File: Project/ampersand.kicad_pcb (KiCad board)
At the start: 2 copper layers, 257.2 x 76.2 mm, 121 parts, among them J1 JST SH, SW1 DFU, U1 STM32F072CBT6, U2 XC6206PxxxMR-Regulator_Linear, U3 74HC4051, U4 OPA354, U5 74HC4051

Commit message: initialise
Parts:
- C11, C12, C14, C6: value 100n -> 100nF
- C7: value 1u -> 1uF
- moved C8 3.97 mm to (92.8, 96.5)
- moved R19 2.72 mm to (199.8, 85.5)
- moved C1 2.58 mm to (91.3, 87.4)
- moved C7 2.58 mm to (91.3, 86.4)
- moved R15 2.45 mm to (198.4, 85.4), turned to 90 degrees
- moved R20 1.71 mm to (197.7, 93.4), turned to -90 degrees
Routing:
- net NRST: track 1.73 -> 5.34 mm
- net +3V3: track 275.4 -> 278.2 mm
- net GND: track 77.1 -> 75.3 mm, vias 418 -> 412
- net COL11: track 161.8 -> 163.3 mm
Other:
- board text added: "6 7 10"
- board text removed: "6 7 8 10"

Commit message: pcb & plate revisions & firmware
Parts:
- added H19: MountingHole, cipulot_parts:HOLE_M2, F.Cu at (69.8, 91.3)
- added H20: MountingHole, cipulot_parts:HOLE_M2, F.Cu at (222.2, 91.3)
- SW_EC40, SW_EC49: footprint cipulot_parts:ecs_pad_no_ring_stepped&normal_cut -> cipulot_parts:ecs_pad_1U_no_ring
- moved SW_EC40 4.76 mm to (60.3, 91.3), turned to -90 degrees
- moved H14 1.59 mm to (88.9, 91.3)
- moved H15 1.59 mm to (203.2, 91.3)
- turned SW_EC49 to -90 degrees
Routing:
- net ROW3: track 397.8 -> 388.7 mm, vias 12 -> 10
- net Net-(U1-PB4): track 46.1 -> 47.4 mm
- net COL10: track 102.7 -> 101.6 mm, vias 5 -> 4
- net COL1: track 72.0 -> 71.6 mm, vias 5 -> 4
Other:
- board text added: "6"
- board text removed: "6 7 10"

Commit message: bottom row change, plate update, firmware update
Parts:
- added H26: MountingHole, cipulot_parts:HOLE_M2, F.Cu at (212.7, 91.3)
- added H27: MountingHole, cipulot_parts:HOLE_M2, F.Cu at (79.4, 91.3)
- moved G*** 75.2 mm to (141.3, 42.9)
- moved H14 33.3 mm to (55.6, 91.3)
- moved SW1 29.0 mm to (186.2, 96.8), turned to 90 degrees
- moved H19 28.6 mm to (98.4, 91.3)
- moved C7 19.6 mm to (109.2, 94.2), turned to 0 degrees
- moved C1 18.8 mm to (109.2, 93.2), turned to 0 degrees
- moved C3 17.9 mm to (111.3, 89.6), turned to 90 degrees
- moved C8 17.6 mm to (109.9, 92.1), turned to 0 degrees
- moved R5 17.3 mm to (111.3, 87.7), turned to -90 degrees
- moved C4 16.8 mm to (109.9, 91.0), turned to 0 degrees
- moved C13 16.3 mm to (101.6, 96.5), turned to 90 degrees
- moved C2 16.0 mm to (110.0, 82.2), turned to -90 degrees
- moved R11 16.0 mm to (107.3, 94.2), turned to 180 degrees
- moved U4 15.3 mm to (104.0, 95.8), turned to 90 degrees
- moved R13 15.1 mm to (107.3, 93.1), turned to 180 degrees
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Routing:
- net Net-(U1-PB6): track 48.2 -> 22.7 mm
- net Net-(U1-PB4): track 47.4 -> 22.1 mm
- net Net-(U1-PB5): track 47.1 -> 22.4 mm
- net Net-(U1-PB3): track 44.9 -> 21.8 mm
- net D_P: track 121.3 -> 105.8 mm
- net D_N: track 117.6 -> 102.8 mm
- net +3V3: track 278.2 -> 264.7 mm, vias 9 -> 8
- net ADC: track 5.95 -> 15.9 mm
- net COL6: track 110.6 -> 101.1 mm
- net COL11: track 163.3 -> 172.5 mm
- net GND: track 75.3 -> 84.0 mm, vias 412 -> 411
- net COL2: track 92.7 -> 101.1 mm
- net BOOT0: track 81.8 -> 89.6 mm
- net AMUX_SEL_0: track 172.7 -> 165.5 mm
- net AMUX_SEL_1: track 171.9 -> 165.0 mm
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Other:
- board text added: "7 10"
- board text removed: "3"
- board text removed: "6"

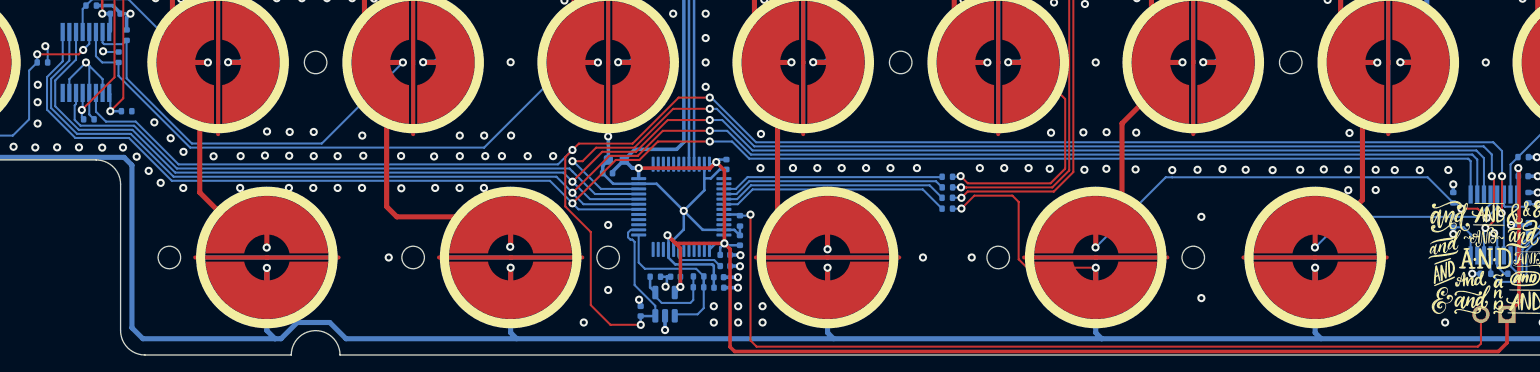
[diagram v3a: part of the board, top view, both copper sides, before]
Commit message: updated production files
naevies plate added
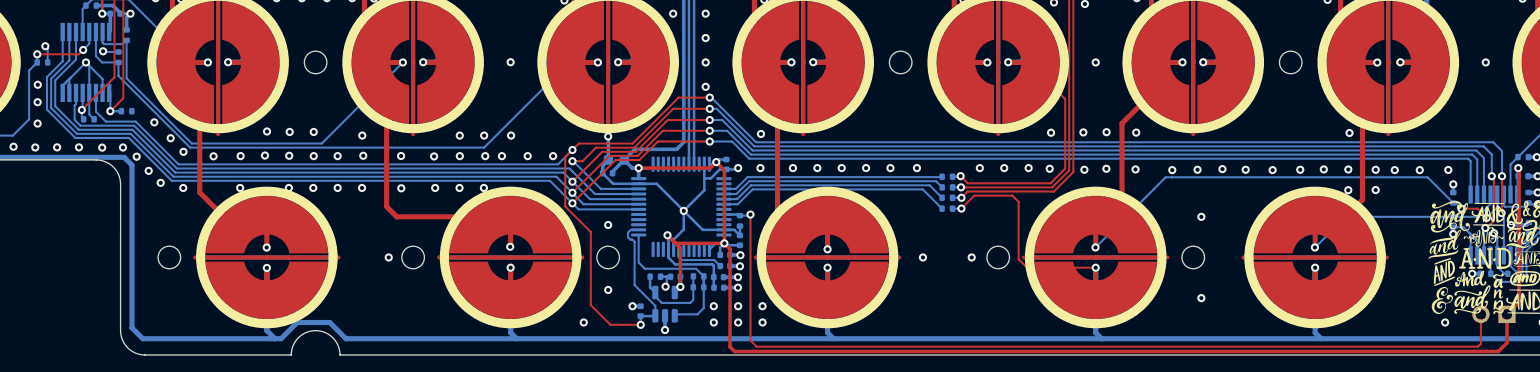
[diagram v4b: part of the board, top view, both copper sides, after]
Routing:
- net GND: track 84.0 -> 89.6 mm, vias 411 -> 412
